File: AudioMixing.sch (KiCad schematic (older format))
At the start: 36 parts, among them U14 MAX98089ETN+

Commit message: Kleinigkeiten
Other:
- note removed: "Oszillator@12.28MHz entfernt, \nda BM83-CODEC, von dem MCLK ausgeht, \nsich als dauerhaft aktiv konfigurieren lässt"
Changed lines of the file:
@@
 Text Label 7850 3350 0    50   ~ 0
 MAX_MICBIAS
-Text Notes 4700 1550 0    50   ~ 0
-HPSNS ist GND an Klinkenbuchse, vgl. Fig 40\nJack sensing nicht vorgesehen -> HPSNS direkt an GND\nMic: differential + biasing\n\nÄnderungen:\nI2C Pullups auf RPi Seite machen\nFootprints angepasst\nSPKRVDD auf 3V3, nicht mehr 5V (siehe DS S.126)\nReihen Cs bei Line Out entfernt (siehe Email Maxim 02.07.2021)\nfix: AGND keine Verbindung zu GND\nfix: EPAD auf GND, nicht NC\nfix: bypass C an Oszilator, wie in Datenblatt gefordert
+Text Notes 4400 1600 0    50   ~ 0
+HPSNS ist GND an Klinkenbuchse, vgl. Fig 40\nJack sensing nicht vorgesehen -> HPSNS direkt an GND\nMic: differential + biasing\n\nÄnderungen:\nI2C Pullups auf RPi Seite machen\nFootprints angepasst\nSPKRVDD auf 3V3, nicht mehr 5V (siehe DS S.126)\nReihen Cs bei Line Out entfernt (siehe Email Maxim 02.07.2021)\nfix: AGND keine Verbindung zu GND\nfix: EPAD auf GND, nicht NC\nfix: bypass C an Oszilator, wie in Datenblatt gefordert\nOszillator@12.28MHz entfernt,  da BM83-CODEC, von dem MCLK ausgeht, \nsich als dauerhaft aktiv konfigurieren lässt
 $Comp
 L power:+3V3 #PWR0124
@@
 Wire Wire Line
 	4550 2450 1700 2450
-Text Notes 5000 6400 0    50   ~ 0
-Oszillator@12.28MHz entfernt, \nda BM83-CODEC, von dem MCLK ausgeht, \nsich als dauerhaft aktiv konfigurieren lässt
 $EndSCHEMATC

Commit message: - Layout MAX98 - Audiostecker Belegung angepasst
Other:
- note added: "1V8 Pegel\nDurch DVDD festgelegt\nmax. 2,0V erlaubt"
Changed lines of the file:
@@
 	1700 2350 4550 2350
 Wire Wire Line
-	10150 2350 7150 2350
+	9200 2350 7150 2350
 Wire Wire Line
 	1700 2650 4550 2650
@@
 Text Notes 600  2800 0    50   ~ 0
 I2S1_Master
-Text HLabel 10150 2350 2    50   Input ~ 0
+Text HLabel 9200 2350 2    50   Input ~ 0
 I2S2_SD_IN
 Text HLabel 1700 2050 0    50   Output ~ 0
@@
 Wire Wire Line
 	4550 2450 1700 2450
+Text Notes 10000 2450 0    50   ~ 0
+1V8 Pegel\nDurch DVDD festgelegt\nmax. 2,0V erlaubt
+Wire Notes Line
+	9900 2050 10950 2050
+Wire Notes Line
+	10950 2050 10950 2750
+Wire Notes Line
+	10950 2750 9900 2750
+Wire Notes Line
+	9900 2750 9900 2050
 $EndSCHEMATC

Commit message: - IRQ Pullup Spannung auf 3,3V
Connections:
- net +1V8: no longer R44.1
- net +3V3: now also R44.1
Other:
- note added: "HPSNS ist GND an Klinkenbuchse, vgl. Fig 40\nJack sensing nicht vorgesehen -> HPSNS direkt an GND\nMic: differential + biasing\n\nÄnderungen:\nIRQ Pullup auf 3,3V statt 1,8V ziehen\nI2C Pullups auf RPi Seite machen\nFootprints angepasst\nSPKRVDD auf 3V3, nicht mehr 5V (siehe DS S.126)\nReihen Cs bei Line Out entfernt (siehe Email Maxim 02.07.2021)\nfix: AGND keine Verbindung zu GND\nfix: EPAD auf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"
- note removed: "1V8 Pegel\nDurch DVDD festgelegt\nmax. 2,0V erlaubt"
- note removed: "HPSNS ist GND an Klinkenbuchse, vgl. Fig 40\nJack sensing nicht vorgesehen -> HPSNS direkt an GND\nMic: differential + biasing\n\nÄnderungen:\nI2C Pullups auf RPi Seite machen\nFootprints angepasst\nSPKRVDD auf 3V3, nicht mehr 5V (siehe DS S.126)\nReihen Cs bei Line Out entfernt (siehe Email Maxim 02.07.2021)\nfix: AGND keine Verbindung zu GND\nfix: EPAD auf GND, nicht NC\nfix: bypass C an Oszila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"
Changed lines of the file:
@@
 Wire Wire Line
 	7350 1700 7350 2250
-$Comp
-L power:+1V8 #PWR0145
-U 1 1 61162E7B
-P 7900 1700
-F 0 "#PWR0145" H 7900 1550 50  0001 C CNN
-F 1 "+1V8" H 7915 1873 50  0000 C CNN
-F 2 "" H 7900 1700 50  0001 C CNN
-F 3 "" H 7900 1700 50  0001 C CNN
-	1    7900 1700
-	1    0    0    -1
-$EndComp
 Wire Wire Line
 	7900 1700 7900 1750
@@
 MAX_MICBIAS
 Text Notes 4400 1600 0    50   ~ 0
-HPSNS ist GND an Klinkenbuchse, vgl. Fig 40\nJack sensing nicht vorgesehen -> HPSNS direkt an GND\nMic: differential + biasing\n\nÄnderungen:\nI2C Pullups auf RPi Seite machen\nFootprints angepasst\nSPKRVDD auf 3V3, nicht mehr 5V (siehe DS S.126)\nReihen Cs bei Line Out entfernt (siehe Email Maxim 02.07.2021)\nfix: AGND keine Verbindung zu GND\nfix: EPAD auf GND, nicht NC\nfix: bypass C an Oszilator, wie in Datenblatt gefordert\nOszillator@12.28MHz entfernt,  da BM83-CODEC, von dem MCLK ausgeht, \nsich als dauerhaft aktiv konfigurieren lässt
+HPSNS ist GND an Klinkenbuchse, vgl. Fig 40\nJack sensing nicht vorgesehen -> HPSNS direkt an GND\nMic: differential + biasing\n\nÄnderungen:\nIRQ Pullup auf 3,3V statt 1,8V ziehen\nI2C Pullups auf RPi Seite machen\nFootprints angepasst\nSPKRVDD auf 3V3, nicht mehr 5V (siehe DS S.126)\nReihen Cs bei Line Out entfernt (siehe Email Maxim 02.07.2021)\nfix: AGND keine Verbindung zu GND\nfix: EPAD auf GND, nicht NC\nfix: bypass C an Oszilator, wie in Datenblatt gefordert\nOszillator@12.28MHz entfernt,  da BM83-CODEC, von dem MCLK ausgeht, \nsich als dauerhaft aktiv konfigurieren lässt
 $Comp
 L power:+3V3 #PWR0124
@@
 Wire Wire Line
 	4550 2450 1700 2450
-Text Notes 10000 2450 0    50   ~ 0
-1V8 Pegel\nDurch DVDD festgelegt\nmax. 2,0V erlaubt
-Wire Notes Line
-	9900 2050 10950 2050
-Wire Notes Line
-	10950 2050 10950 2750
-Wire Notes Line
-	10950 2750 9900 2750
-Wire Notes Line
-	9900 2750 9900 2050
+$Comp
+L power:+3V3 #PWR0145
+U 1 1 61D9B108
+P 7900 1700
+F 0 "#PWR0145" H 7900 1550 50  0001 C CNN
+F 1 "+3V3" H 7915 1873 50  0000 C CNN
+F 2 "" H 7900 1700 50  0001 C CNN
+F 3 "" H 7900 1700 50  0001 C CNN
+	1    7900 1700
+	1    0    0    -1
+$EndComp
 $EndSCHEMATC

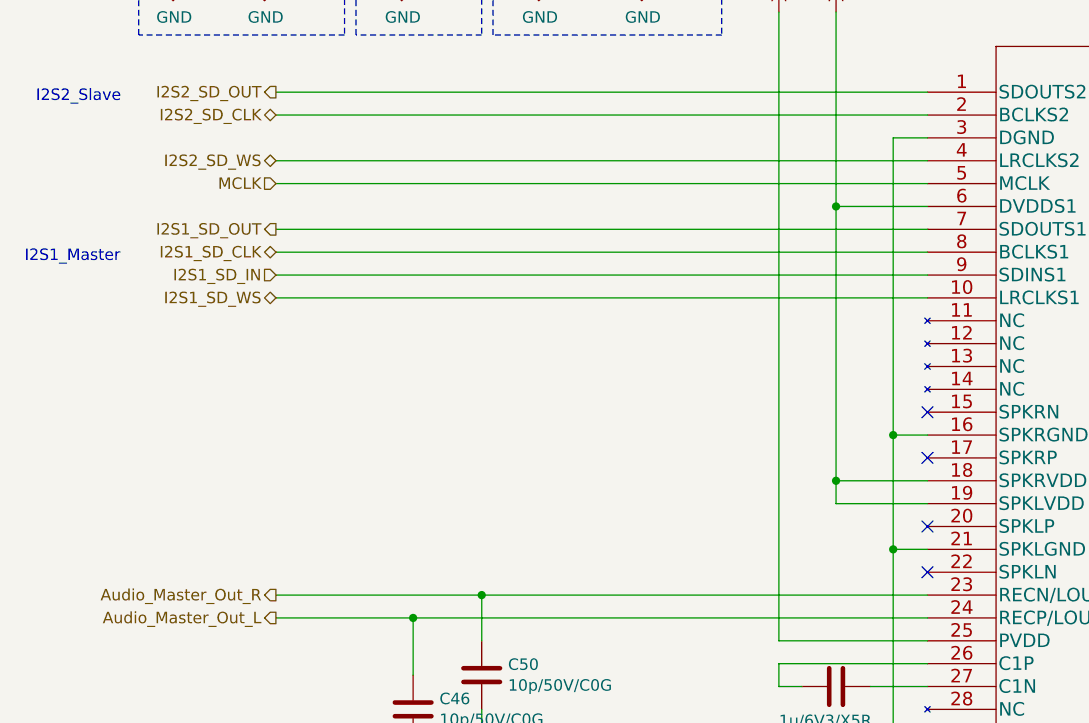
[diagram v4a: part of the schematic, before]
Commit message: - Schaltplan und BOM an BM64 angepasst
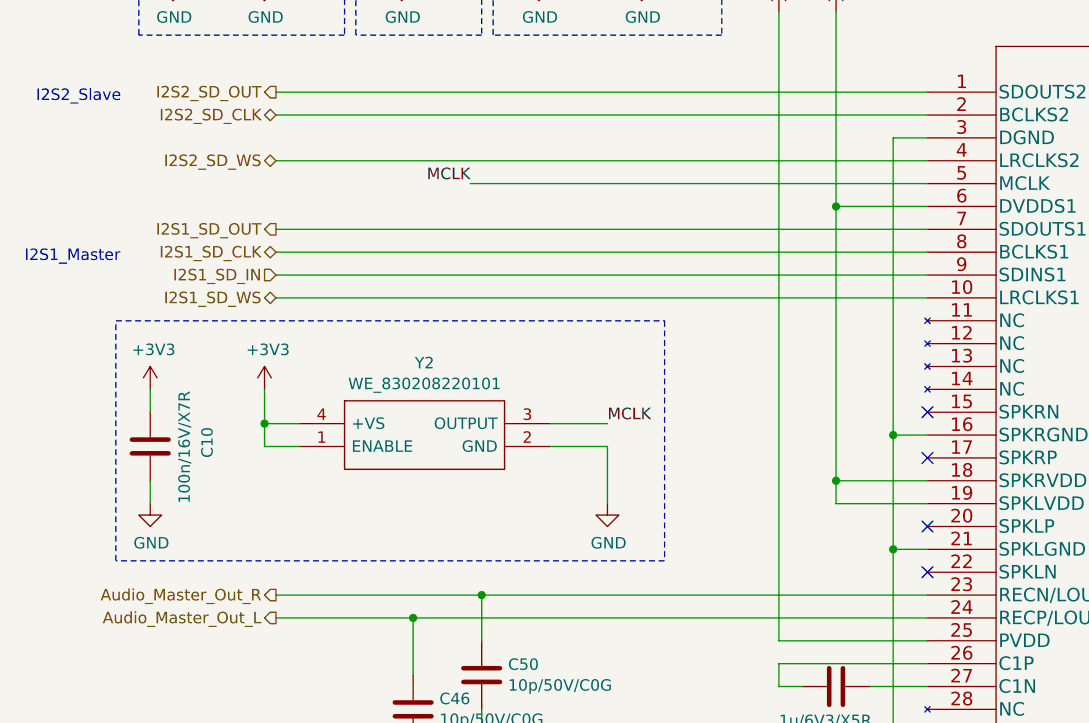
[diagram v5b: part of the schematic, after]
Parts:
- added C10: 100n/16V/X7R, Capacitor_SMD:C_0402_1005Metric, symbol Device:C
- added Y2: WE_830208220101, TeKaDe:WE_IQXO-791, symbol TeKaDe:WE_830208220101
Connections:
- net +3V3: now also C10.1, Y2.1 (ENABLE), Y2.4 (+VS)
- net GND: now also C10.2, Y2.2 (GND)
- net MCLK: now also Y2.3 (OUTPUT)
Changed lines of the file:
@@
 Text HLabel 1700 2350 0    50   BiDi ~ 0
 I2S2_SD_WS
-Text HLabel 1700 2450 0    50   Input ~ 0
-MCLK
-Wire Wire Line
-	4550 2450 1700 2450
+Wire Wire Line
+	4550 2450 2550 2450
 $Comp
 L power:+3V3 #PWR0145
@@
 	-1   0    0    -1
 $EndComp
+Text Label 2550 2450 2    50   ~ 0
+MCLK
+$Comp
+L TeKaDe:WE_830208220101 Y2
+U 1 1 624E0C4D
+P 1200 3500
+F 0 "Y2" H 2350 3765 50  0000 C CNN
+F 1 "WE_830208220101" H 2350 3674 50  0000 C CNN
+F 2 "TeKaDe:WE_IQXO-791" H 2750 3600 50  0001 L CNN
+F 3 "https://www.we-online.de/katalog/datasheet/830208220101.pdf" H 2750 3500 50  0001 L CNN
+F 4 "Standard 2.5 x 2.0 oscillator in a ceramic package with a hermetically sealed metal lid." H 2750 3400 50  0001 L CNN "Description"
+F 5 "1" H 2750 3300 50  0001 L CNN "Height"
+F 6 "Wurth Elektronik" H 2750 3000 50  0001 L CNN "Manufacturer_Name"
+F 7 "830208220101" H 2750 2900 50  0001 L CNN "Manufacturer_Part_Number"
+	1    1200 3500
+	1    0    0    -1
+$EndComp
+$Comp
+L power:GND #PWR0112
+U 1 1 624E26F0
+P 3150 3850
+F 0 "#PWR0112" H 3150 3600 50  0001 C CNN
+F 1 "GND" H 3155 3677 50  0000 C CNN
+F 2 "" H 3150 3850 50  0001 C CNN
+F 3 "" H 3150 3850 50  0001 C CNN
+	1    3150 3850
+	1    0    0    -1
+$EndComp
+$Comp
+L Device:C C10
+U 1 1 624E2F8D
+P 1150 3600
+F 0 "C10" V 1400 3550 50  0000 L CNN
+F 1 "100n/16V/X7R" V 1300 3350 50  0000 L CNN
+F 2 "Capacitor_SMD:C_0402_1005Metric" H 1188 3450 50  0001 C CNN
+F 3 "~" H 1150 3600 50  0001 C CNN
+	1    1150 3600
+	1    0    0    -1
+$EndComp
+$Comp
+L power:+3V3 #PWR0174
+U 1 1 624E36F3
+P 1150 3350
+F 0 "#PWR0174" H 1150 3200 50  0001 C CNN
+F 1 "+3V3" H 1165 3523 50  0000 C CNN
+F 2 "" H 1150 3350 50  0001 C CNN
+F 3 "" H 1150 3350 50  0001 C CNN
+	1    1150 3350
+	1    0    0    -1
+$EndComp
+$Comp
+L power:+3V3 #PWR0175
+U 1 1 624E400D
+P 1650 3350
+F 0 "#PWR0175" H 1650 3200 50  0001 C CNN
+F 1 "+3V3" H 1665 3523 50  0000 C CNN
+F 2 "" H 1650 3350 50  0001 C CNN
+F 3 "" H 1650 3350 50  0001 C CNN
+	1    1650 3350
+	1    0    0    -1
+$EndComp
+$Comp
+L power:GND #PWR0191
+U 1 1 624E4364
+P 1150 3850
+F 0 "#PWR0191" H 1150 3600 50  0001 C CNN
+F 1 "GND" H 1155 3677 50  0000 C CNN
+F 2 "" H 1150 3850 50  0001 C CNN
+F 3 "" H 1150 3850 50  0001 C CNN
+	1    1150 3850
+	1    0    0    -1
+$EndComp
+Wire Wire Line
+	2900 3600 3150 3600
+Wire Wire Line
+	3150 3600 3150 3850
+Wire Wire Line
+	1650 3350 1650 3500
+Wire Wire Line
+	1650 3600 1800 3600
+Wire Wire Line
+	1800 3500 1650 3500
+Connection ~ 1650 3500
+Wire Wire Line
+	1650 3500 1650 3600
+Wire Wire Line
+	1150 3350 1150 3450
+Wire Wire Line
+	1150 3750 1150 3850
+Text Label 3150 3500 0    50   ~ 0
+MCLK
+Wire Wire Line
+	3150 3500 2900 3500
+Wire Notes Line
+	1000 3050 3400 3050
+Wire Notes Line
+	3400 3050 3400 4100
+Wire Notes Line
+	3400 4100 1000 4100
+Wire Notes Line
+	1000 4100 1000 3050
 $EndSCHEMATC

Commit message: layout first try
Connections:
- net I2S1_SD_IN is gone; now on net GND: U14.9 (SDINS1)
- net I2S1_SD_CLK: no longer names the net of U14.8 (BCLKS1)
- net I2S1_SD_OUT: no longer names the net of U14.7 (SDOUTS1)
- net I2S1_SD_WS: no longer names the net of U14.10 (LRCLKS1)
- no-connect marks 7 -> 10
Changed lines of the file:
@@
 $Descr A4 11693 8268
 encoding utf-8
-Sheet 6 8
+Sheet 5 6
 Title ""
 Date ""
@@
 	4400 2250 4550 2250
 Wire Wire Line
-	4400 2250 4400 3550
+	4400 2250 4400 2850
 NoConn ~ 4550 3450
 NoConn ~ 4550 3650
@@
 Wire Wire Line
 	9200 2350 7150 2350
-Wire Wire Line
-	1700 2650 4550 2650
-Wire Wire Line
-	1700 2750 4550 2750
-Wire Wire Line
-	1700 2850 4550 2850
 Wire Wire Line
 	2600 4450 2600 4250
@@
 Text HLabel 10150 2650 2    50   Input ~ 0
 I2C_SCL
-Text HLabel 1700 2850 0    50   Input ~ 0
-I2S1_SD_IN
-Text HLabel 1700 2650 0    50   Output ~ 0
-I2S1_SD_OUT
-Text HLabel 1700 2750 0    50   BiDi ~ 0
-I2S1_SD_CLK
-Wire Wire Line
-	1700 2950 4550 2950
-Text HLabel 1700 2950 0    50   BiDi ~ 0
-I2S1_SD_WS
 Text Notes 650  2100 0    50   ~ 0
 I2S2_Slave
@@
 Wire Notes Line
 	1000 4100 1000 3050
+NoConn ~ 4550 2650
+NoConn ~ 4550 2750
+NoConn ~ 4550 2950
+Wire Wire Line
+	4550 2850 4400 2850
+Connection ~ 4400 2850
+Wire Wire Line
+	4400 2850 4400 3550
 $EndSCHEMATC
